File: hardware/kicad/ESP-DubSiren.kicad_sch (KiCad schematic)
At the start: 64 parts, among them J1 USB4085-GF-A, J2 RCJ-2123, SW1 MX2A-11NW, SW2 MX2A-11NW, SW3 MX2A-11NW, SW4 MX2A-11NW, SW5 RESET, SW6 BOOT, SW7 PEC11R-4120F-S0018, U1 ESP32-S3-WROOM-1U-N16R8, U2 MPM3612GLQ-33-Z, U3 74HC4051D, U4 USBLC6-2SC6, U5 Adafruit 5393, U6 Adafruit 6250, U7 TPS22918DBVR

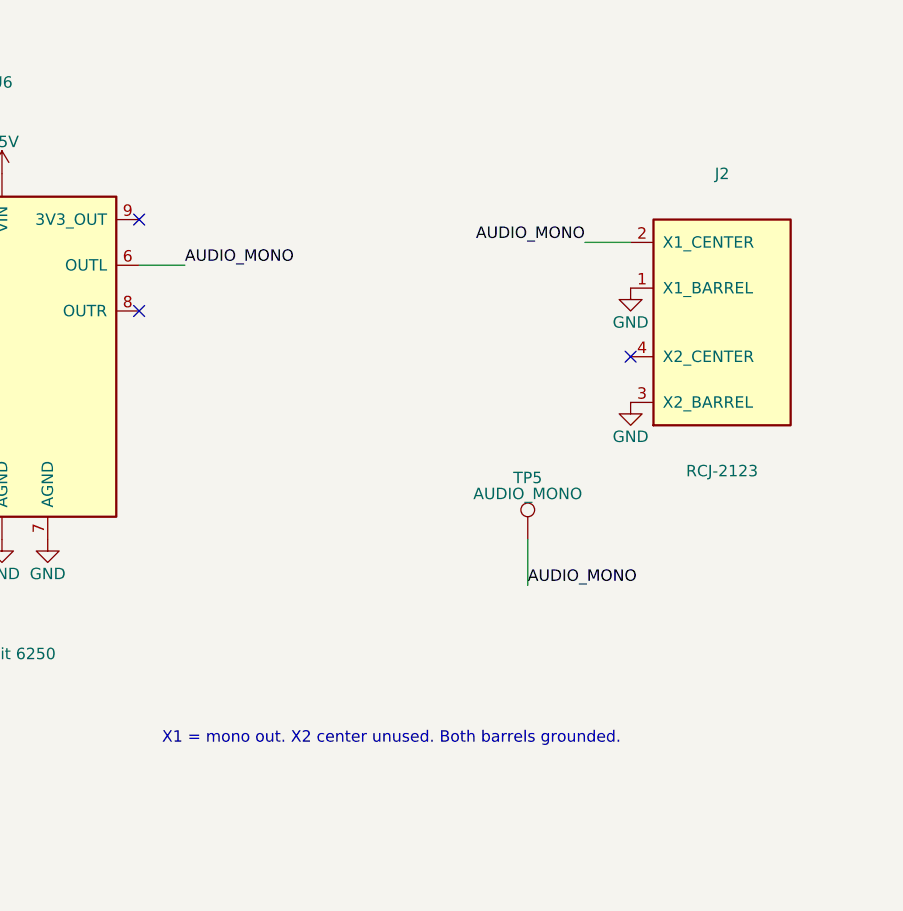
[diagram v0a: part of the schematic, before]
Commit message: Replace RCA with NRJ4HF and document rear mechanical study
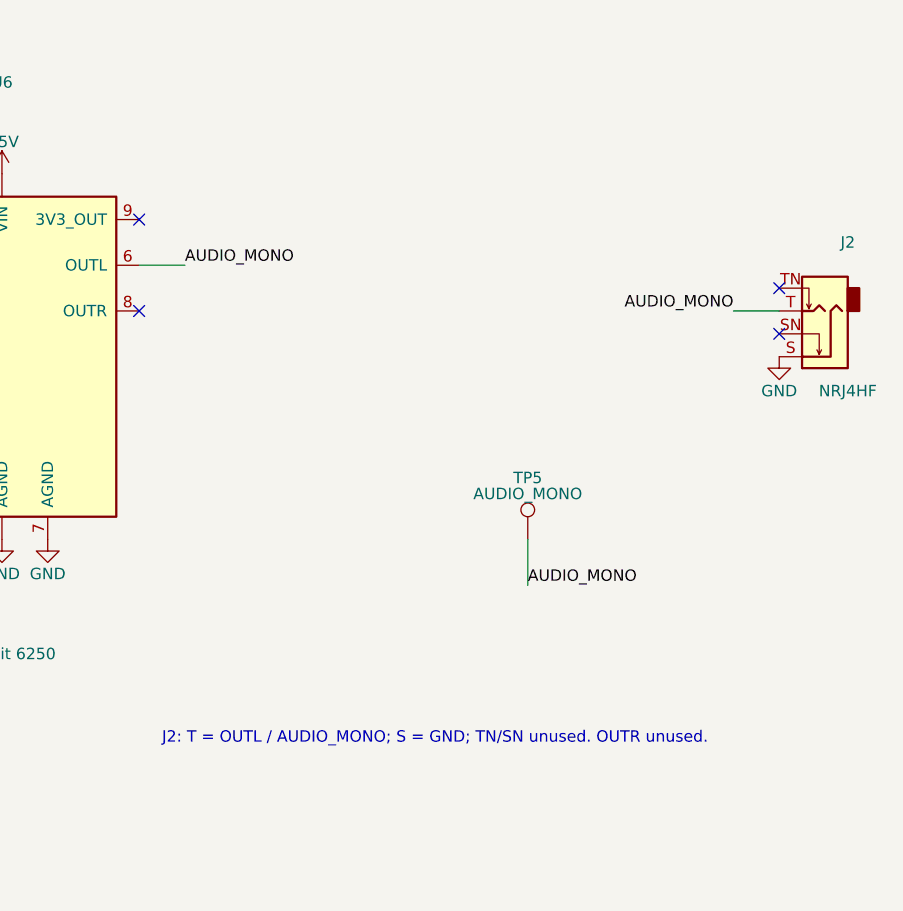
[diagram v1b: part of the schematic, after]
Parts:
- J2: value RCJ-2123 -> NRJ4HF; footprint ESP-DubSiren-V2-Mechanical:SameSky_RCJ-2123 -> Connector_Audio:Jack_6.35mm_Neutrik_NRJ4HF_Horizontal; symbol ESP-DubSiren-V2:RCJ-2123 -> Connector_Audio:AudioJack2_Switch; MPN RCJ-2123 -> NRJ4HF; Manufacturer Same Sky -> Neutrik
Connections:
- net AUDIO_MONO: now also J2.T; no longer J2.2 (X1_CENTER)
- net GND: now also J2.S; no longer J2.1 (X1_BARREL), J2.3 (X2_BARREL)
- no-connect marks 27 -> 28
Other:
- note added: "J2: T = OUTL / AUDIO_MONO; S = GND; TN/SN unused. OUTR unused."
- note removed: "X1 = mono out. X2 center unused. Both barrels grounded."
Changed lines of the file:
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@@
 	)
 	(no_connect
-		(at 544.83 132.08)
+		(at 193.04 93.98)
 	)
 	(no_connect
-		(at 193.04 93.98)
+		(at 561.34 129.54)
+	)
+	(no_connect
+		(at 561.34 124.46)
 	)
 	(wire
@@
 	(wire
 		(pts
-			(xy 544.83 119.38)
-			(xy 539.75 119.38)
-		)
-	)
-	(wire
-		(pts
 			(xy 241.3 109.22)
 			(xy 236.22 109.22)
@@
 		)
 	)
+	(wire
+		(pts
+			(xy 561.34 127)
+			(xy 556.26 127)
+		)
+	)
 	(text "USB-C / input protection"
 		(at 20.32 15.24 0)
@@
 		)
 	)
-	(text "X1 = mono out. X2 center unused. Both barrels grounded."
-		(at 492.76 175.26 0)
+	(text "PROTOTYPE - all controls populated; USB power policy and bench qualification pending"
+		(at 20.32 360.68 0)
 		(effects
 			(font
@@
 		)
 	)
-	(label "AUDIO_MONO"
-		(at 539.75 119.38 180)
-		(effects
-			(font
-				(size 1.27 1.27)
-			)
-			(justify right bottom)
-		)
-	)
 	(label "ESP_EN"
 		(at 236.22 109.22 180)
@@
 		)
 	)
-  (text "PROTOTYPE - all controls populated; USB power policy and bench qualification pending"
-    (at 20.32 360.68 0)
+	(label "AUDIO_MONO"
+		(at 556.26 127 180)
+		(effects
+			(font
+				(size 1.27 1.27)
+			)
+			(justify right bottom)
+		)
+	)
+  (text "J2: T = OUTL / AUDIO_MONO; S = GND; TN/SN unused. OUTR unused."
+    (at 492.76 175.26 0)
     (effects (font (size 1.27 1.27)) (justify left bottom))
   )
@@
 	)
 	(symbol
-		(lib_id "ESP-DubSiren-V2:RCJ-2123")
-		(at 566.42 127 0)
+		(lib_id "Connector_Audio:AudioJack2_Switch")
+		(at 566.42 127 180)
 		(unit 1)
 		(in_bom yes)
@@
 		(dnp no)
 		(property "Reference" "J2"
-			(at 554.99 111.76 0)
+			(at 568.96 119.38 0)
 			(effects
 				(font
@@
 			)
 		)
-		(property "Value" "RCJ-2123"
-			(at 554.99 144.78 0)
+		(property "Value" "NRJ4HF"
+			(at 568.96 135.89 0)
 			(effects
 				(font
@@
 			)
 		)
-		(property "Footprint" "ESP-DubSiren-V2-Mechanical:SameSky_RCJ-2123"
+		(property "Footprint" "Connector_Audio:Jack_6.35mm_Neutrik_NRJ4HF_Horizontal"
 			(at 566.42 127 0)
 			(hide yes)
@@
 			)
 		)
-		(property "Datasheet" "https://www.sameskydevices.com/product/resource/rcj-21.pdf"
+		(property "Datasheet" "https://www.neutrik.com/media/8561/download/st-nrj4hf.PDF?v=2"
 			(at 566.42 127 0)
 			(hide yes)
@@
 			)
 		)
-		(property "MPN" "RCJ-2123"
+		(property "MPN" "NRJ4HF"
 			(at 566.42 127 0)
 			(hide yes)
@@
 			)
 		)
-		(property "Manufacturer" "Same Sky"
+		(property "Manufacturer" "Neutrik"
 			(at 566.42 127 0)
 			(hide yes)
@@
 	(symbol
 		(lib_id "power:GND")
-		(at 544.83 124.46 0)
-		(unit 1)
-		(in_bom yes)
-		(on_board yes)
-		(dnp no)
-		(property "Reference" "#PWR067"
-			(at 544.83 130.81 0)
-			(hide yes)
-			(effects
-				(font
-					(size 1.27 1.27)
-				)
-			)
-		)
-		(property "Value" "GND"
-			(at 544.83 128.27 0)
-			(effects
-				(font
-					(size 1.27 1.27)
-				)
-			)
-		)
-		(property "Footprint" ""
-			(at 544.83 124.46 0)
-			(hide yes)
-			(effects
-				(font
-					(size 1.27 1.27)
-				)
-			)
-		)
-		(property "Datasheet" ""
-			(at 544.83 124.46 0)
-			(hide yes)
-			(effects
-				(font
-					(size 1.27 1.27)
-				)
-			)
-		)
-		(property "Description" "Power symbol creates a global label with name \"GND\" , ground"
-			(at 544.83 124.46 0)
-			(hide yes)
-			(effects
-				(font
-					(size 1.27 1.27)
-				)
-			)
-		)
-		(instances
-			(project "ESP-DubSiren"
-				(path "/2037f81d-e33e-4c09-903b-90b25af374ad"
-					(reference "#PWR067")
-					(unit 1)
-				)
-			)
-		)
-	)
-	(symbol
-		(lib_id "power:GND")
-		(at 544.83 137.16 0)
-		(unit 1)
-		(in_bom yes)
-		(on_board yes)
-		(dnp no)
-		(property "Reference" "#PWR068"
-			(at 544.83 143.51 0)
-			(hide yes)
-			(effects
-				(font
-					(size 1.27 1.27)
-				)
-			)
-		)
-		(property "Value" "GND"
-			(at 544.83 140.97 0)
-			(effects
-				(font
-					(size 1.27 1.27)
-				)
-			)
-		)
-		(property "Footprint" ""
-			(at 544.83 137.16 0)
-			(hide yes)
-			(effects
-				(font
-					(size 1.27 1.27)
-				)
-			)
-		)
-		(property "Datasheet" ""
-			(at 544.83 137.16 0)
-			(hide yes)
-			(effects
-				(font
-					(size 1.27 1.27)
-				)
-			)
-		)
-		(property "Description" "Power symbol creates a global label with name \"GND\" , ground"
-			(at 544.83 137.16 0)
-			(hide yes)
-			(effects
-				(font
-					(size 1.27 1.27)
-				)
-			)
-		)
-		(instances
-			(project "ESP-DubSiren"
-				(path "/2037f81d-e33e-4c09-903b-90b25af374ad"
-					(reference "#PWR068")
-					(unit 1)
-				)
-			)
-		)
-	)
-	(symbol
-		(lib_id "power:GND")
 		(at 251.46 109.22 0)
 		(unit 1)
@@
 			)
 		)
+		(property "MPN" "MX2A-11NW"
+			(at 515.62 259.08 0)
+			(hide yes)
+			(effects
+				(font
+					(size 1.27 1.27)
+				)
+			)
+		)
+		(property "Manufacturer" "CHERRY"
+			(at 515.62 259.08 0)
+			(hide yes)
+			(effects
+				(font
+					(size 1.27 1.27)
+				)
+			)
+		)
 		(instances
 			(project "ESP-DubSiren"
@@
 			)
 		)
-		(property "MPN" "MX2A-11NW"
-			(at 515.62 259.08 0)
+	)
+	(symbol
+		(lib_id "power:GND")
+		(at 561.34 132.08 0)
+		(unit 1)
+		(in_bom yes)
+		(on_board yes)
+		(dnp no)
+		(property "Reference" "#PWR067"
+			(at 561.34 138.43 0)
 			(hide yes)
 			(effects
@@
 			)
 		)
-		(property "Manufacturer" "CHERRY"
-			(at 515.62 259.08 0)
+		(property "Value" "GND"
+			(at 561.34 135.89 0)
+			(effects
+				(font
+					(size 1.27 1.27)
+				)
+			)
+		)
+		(property "Footprint" ""
+			(at 561.34 132.08 0)
 			(hide yes)
 			(effects
@@
 				)
 			)
-		))
+		)
+		(property "Datasheet" ""
+			(at 561.34 132.08 0)
+			(hide yes)
+			(effects
+				(font
+					(size 1.27 1.27)
+				)
+			)
+		)
+		(property "Description" "Power symbol creates a global label with name \"GND\" , ground"
+			(at 561.34 132.08 0)
+			(hide yes)
+			(effects
+				(font
+					(size 1.27 1.27)
+				)
+			)
+		)
+		(instances
+			(project "ESP-DubSiren"
+				(path "/2037f81d-e33e-4c09-903b-90b25af374ad"
+					(reference "#PWR067")
+					(unit 1)
+				)
+			)
+		)
+	)
 )
